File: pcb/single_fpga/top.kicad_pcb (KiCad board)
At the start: 2 copper layers, 320 x 320 mm, 208 parts, among them J1 AXK680337YG, J2 AXK680337YG, J3 AXK680337YG, J4 AXK680337YG, U1 Comment, U10 Comment, U11 Comment, U12 Comment, U13 Comment, U14 Comment, U15 Comment, U16 Comment, U17 Comment, U18 Comment, U19 Comment, U2 Comment, U20 Comment, U21 Comment, U22 Comment, U23 Comment, U24 Comment, U25 Comment, U26 Comment, U27 Comment, U28 Comment, U29 Comment, U3 Comment, U30 Comment, U31 Comment, U32 Comment, U33 Comment, U34 Comment, U35 Comment, U36 Comment, U37 Comment, U38 Comment, U39 Comment, U4 Comment, U40 Comment, U41 Comment, U42 Comment, U43 Comment, U44 Comment, U45 Comment, U46 Comment, U47 Comment, U48 Comment, U49 Comment, U5 Comment, U50 Comment, U51 Comment, U52 Comment, U53 Comment, U54 Comment, U55 Comment, U56 Comment, U57 Comment, U58 Comment, U59 Comment, U6 Comment, U60 Comment, U61 Comment, U62 Comment, U63 Comment, U64 Comment, U65 Comment, U66 Comment, U67 Comment, U68 Comment, U69 Comment, U7 Comment, U70 Comment, U71 Comment, U72 Comment, U73 Comment, U74 Comment, U75 Comment, U76 Comment, U77 Comment, U78 Comment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

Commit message: Fixed mounting holes for Rpi Cam3 Wide.
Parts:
- moved HCAM1 7.97 mm to (258.4, 205.4)
- moved HCAM2 7.97 mm to (279.4, 205.4)
- moved HCAM3 6.20 mm to (258.4, 217.9)
- moved HCAM4 6.20 mm to (279.4, 217.9)
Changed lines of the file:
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@@
 	(footprint "MountingHole_2.2mm_M2"
 		(layer "F.Cu")
-		(at 276.062916 212.612916)
+		(at 279.362916 217.862916)
 		(descr "Mounting Hole 2.2mm, M2, no annular, generated by kicad-footprint-generator mountinghole.py")
 		(tags "mountinghole M2")
@@
 	(footprint "MountingHole_2.2mm_M2"
 		(layer "F.Cu")
-		(at 261.662916 198.112916)
+		(at 258.362915 205.362916)
 		(descr "Mounting Hole 2.2mm, M2, no annular, generated by kicad-footprint-generator mountinghole.py")
 		(tags "mountinghole M2")
@@
 	(footprint "MountingHole_2.2mm_M2"
 		(layer "F.Cu")
-		(at 276.062916 198.112916)
+		(at 279.362916 205.362916)
 		(descr "Mounting Hole 2.2mm, M2, no annular, generated by kicad-footprint-generator mountinghole.py")
 		(tags "mountinghole M2")
@@
 	(footprint "MountingHole_2.2mm_M2"
 		(layer "F.Cu")
-		(at 261.662916 212.612916)
+		(at 258.362915 217.862916)
 		(descr "Mounting Hole 2.2mm, M2, no annular, generated by kicad-footprint-generator mountinghole.py")
 		(tags "mountinghole M2")

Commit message: Fixed.
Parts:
- added U100: PW0016A_N, PW0016A_N, F.Cu at (44.9, 75.0)
- added U101: PW0016A_N, PW0016A_N, F.Cu at (1.34, 87.4)
- added U102: PW0016A_N, PW0016A_N, F.Cu at (-42.5, 76.4)
- added U103: PW0016A_N, PW0016A_N, F.Cu at (-75.0, 44.9)
- added U104: PW0016A_N, PW0016A_N, F.Cu at (-87.4, 1.34)
- added U105: PW0016A_N, PW0016A_N, F.Cu at (-76.4, -42.5)
- added U106: PW0016A_N, PW0016A_N, F.Cu at (-44.9, -75.0)
- added U107: PW0016A_N, PW0016A_N, F.Cu at (-1.34, -87.4)
- added U108: PW0016A_N, PW0016A_N, F.Cu at (42.5, -76.4)
- added U109: PW0016A_N, PW0016A_N, F.Cu at (75.0, -44.9)
- added U110: PW0016A_N, PW0016A_N, F.Cu at (87.4, -1.34)
- added U99: PW0016A_N, PW0016A_N, F.Cu at (76.4, 42.5)

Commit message: Placed 1:8 clock drivers.
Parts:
- U100, U101, U102, U103, U104, U105, U106, U107, U108, U109, U110, U99: footprint PW0016A_N -> CDCLVC1108:PW0016A_N
- moved U101 338.3 mm to (270.2, 292.8)
- moved U109 338.3 mm to (343.9, 160.5)
- moved U100 338.3 mm to (313.7, 280.4)
- moved U103 338.3 mm to (193.8, 250.2)
- moved U104 338.3 mm to (181.4, 206.7)
- moved U106 338.3 mm to (224.0, 130.3)
- moved U107 338.3 mm to (267.5, 117.9)
- moved U108 338.3 mm to (311.4, 129.0)
- moved U99 338.3 mm to (345.2, 247.9)
- moved U102 338.3 mm to (226.3, 281.7)
- moved U105 338.3 mm to (192.5, 162.8)
- moved U110 338.3 mm to (356.3, 204.0)

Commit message: Rotated clock drivers to all up.
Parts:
- turned U104 to 0 degrees
- turned U101 to 0 degrees
- turned U107 to 0 degrees
- turned U110 to 0 degrees
- turned U100 to 0 degrees
- turned U102 to 0 degrees
- turned U103 to 0 degrees
- turned U105 to 0 degrees
- turned U106 to 0 degrees
- turned U108 to 0 degrees
- turned U109 to 0 degrees
- turned U99 to 0 degrees

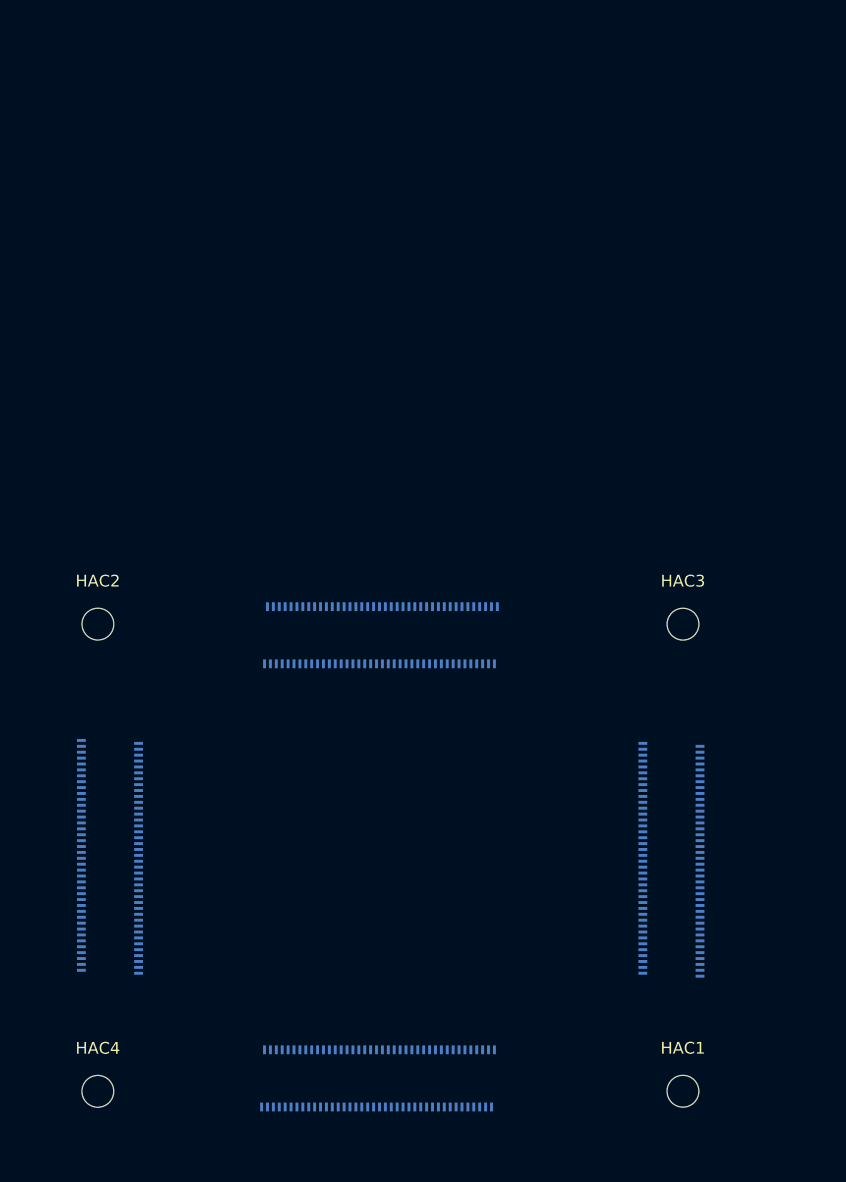
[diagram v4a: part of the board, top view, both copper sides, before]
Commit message: Reorganized sheets for two-boards. Fixed connector off-grid problems.
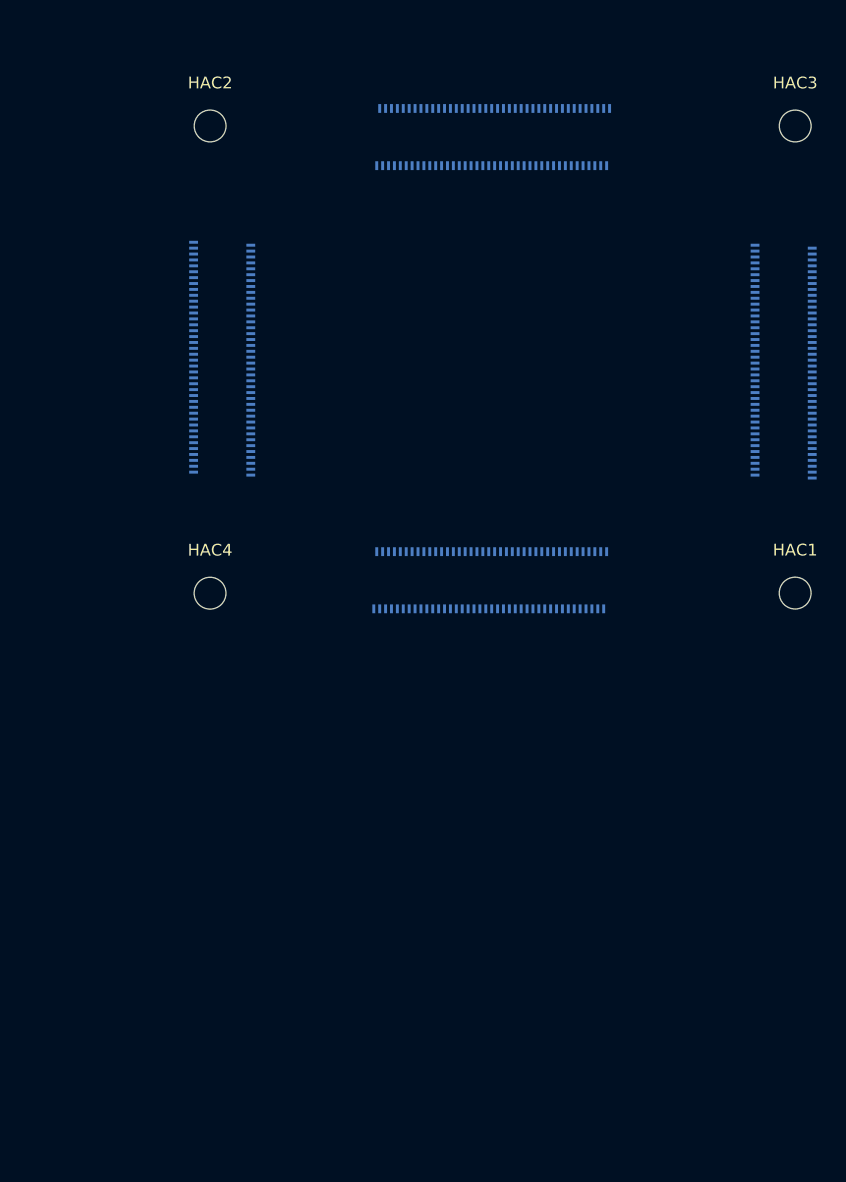
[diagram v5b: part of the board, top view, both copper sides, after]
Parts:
- moved HAC1 43.3 mm to (553.1, 237.7)
- moved HAC2 43.3 mm to (503.5, 198.1)
- moved HAC3 43.3 mm to (553.1, 198.1)
- moved HAC4 43.3 mm to (503.5, 237.7)
- moved J2 43.3 mm to (527.4, 236.6)
- moved J3 43.3 mm to (504.5, 217.9)
- moved J4 43.3 mm to (527.4, 199.0)
- moved J1 43.3 mm to (552.1, 217.9)
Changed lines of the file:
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@@
 	(footprint "MountingHole_2.7mm_M2.5"
 		(layer "F.Cu")
-		(at 543.585321 279.958505)
+		(at 553.104136 237.70183)
 		(descr "Mounting Hole 2.7mm, M2.5, no annular, generated by kicad-footprint-generator mountinghole.py")
 		(tags "mountinghole M2.5")
@@
 	(footprint "MountingHole_2.7mm_M2.5"
 		(layer "F.Cu")
-		(at 493.953721 279.966104)
+		(at 503.472536 237.709429)
 		(descr "Mounting Hole 2.7mm, M2.5, no annular, generated by kicad-footprint-generator mountinghole.py")
 		(tags "mountinghole M2.5")
@@
 	(footprint "MountingHole_2.7mm_M2.5"
 		(layer "F.Cu")
-		(at 493.958821 240.334504)
+		(at 503.477636 198.077829)
 		(descr "Mounting Hole 2.7mm, M2.5, no annular, generated by kicad-footprint-generator mountinghole.py")
 		(tags "mountinghole M2.5")
@@
 	(footprint "MountingHole_2.7mm_M2.5"
 		(layer "F.Cu")
-		(at 543.590421 240.337004)
+		(at 553.109236 198.080329)
 		(descr "Mounting Hole 2.7mm, M2.5, no annular, generated by kicad-footprint-generator mountinghole.py")
 		(tags "mountinghole M2.5")
@@
 	(footprint "AXK680337YG"
 		(layer "B.Cu")
-		(at 517.842422 241.276804)
+		(at 527.361237 199.020129)
 		(descr "Panasonic AXK680337YG P5K-series 80-pin/0.5mm-pitch board-to-board HEADER, 3.0mm mated height. Real dimensions from Panasonic/Mouser's own P5K/P5KS catalog PDF (mouser.com/catalog/specsheets/AXK.pdf), read directly: body 23.20 x 4.60mm (A x width), pin field 19.50mm (B, = (40-1)*0.5mm exactly). Land pattern real: 40 pins/row x 2 rows, 0.5mm pitch, rows staggered by 0.25mm (half pitch, per the catalog's own 'Recommended PC board pattern' drawing), pad 0.25 x 0.75mm, total footprint span 5.60mm (consistent across every land-pattern drawing in the catalog). Pin numbering (1-80 sequential by row) is an ASSUMED convention, not independently verified against a real pin-1 diagram -- the catalog's own orientation key is a chamfered body corner (reproduced here on F.SilkS near pin 1) rather than a numbered pinout drawing. Mates with the ALINX AC7200 module's own AXK580137YG sockets (module-side part number CONFIRMED via ALINX's real schematic, docs/AC7200_Schematic.pdf page 12) -- see ../AC7200/AC7200_README.md.")
 		(tags "Panasonic AXK680337YG P5K board-to-board 80pin 0.5mm")
@@
 	(footprint "AXK680337YG"
 		(layer "B.Cu")
-		(at 494.982421 260.199804 90)
+		(at 504.501236 217.943129 90)
 		(descr "Panasonic AXK680337YG P5K-series 80-pin/0.5mm-pitch board-to-board HEADER, 3.0mm mated height. Real dimensions from Panasonic/Mouser's own P5K/P5KS catalog PDF (mouser.com/catalog/specsheets/AXK.pdf), read directly: body 23.20 x 4.60mm (A x width), pin field 19.50mm (B, = (40-1)*0.5mm exactly). Land pattern real: 40 pins/row x 2 rows, 0.5mm pitch, rows staggered by 0.25mm (half pitch, per the catalog's own 'Recommended PC board pattern' drawing), pad 0.25 x 0.75mm, total footprint span 5.60mm (consistent across every land-pattern drawing in the catalog). Pin numbering (1-80 sequential by row) is an ASSUMED convention, not independently verified against a real pin-1 diagram -- the catalog's own orientation key is a chamfered body corner (reproduced here on F.SilkS near pin 1) rather than a numbered pinout drawing. Mates with the ALINX AC7200 module's own AXK580137YG sockets (module-side part number CONFIRMED via ALINX's real schematic, docs/AC7200_Schematic.pdf page 12) -- see ../AC7200/AC7200_README.md.")
 		(tags "Panasonic AXK680337YG P5K board-to-board 80pin 0.5mm")
@@
 	(footprint "AXK680337YG"
 		(layer "B.Cu")
-		(at 542.607421 260.199804 -90)
+		(at 552.126236 217.943129 -90)
 		(descr "Panasonic AXK680337YG P5K-series 80-pin/0.5mm-pitch board-to-board HEADER, 3.0mm mated height. Real dimensions from Panasonic/Mouser's own P5K/P5KS catalog PDF (mouser.com/catalog/specsheets/AXK.pdf), read directly: body 23.20 x 4.60mm (A x width), pin field 19.50mm (B, = (40-1)*0.5mm exactly). Land pattern real: 40 pins/row x 2 rows, 0.5mm pitch, rows staggered by 0.25mm (half pitch, per the catalog's own 'Recommended PC board pattern' drawing), pad 0.25 x 0.75mm, total footprint span 5.60mm (consistent across every land-pattern drawing in the catalog). Pin numbering (1-80 sequential by row) is an ASSUMED convention, not independently verified against a real pin-1 diagram -- the catalog's own orientation key is a chamfered body corner (reproduced here on F.SilkS near pin 1) rather than a numbered pinout drawing. Mates with the ALINX AC7200 module's own AXK580137YG sockets (module-side part number CONFIRMED via ALINX's real schematic, docs/AC7200_Schematic.pdf page 12) -- see ../AC7200/AC7200_README.md.")
 		(tags "Panasonic AXK680337YG P5K board-to-board 80pin 0.5mm")
@@
 	(footprint "AXK680337YG"
 		(layer "B.Cu")
-		(at 517.842422 278.868804 180)
+		(at 527.361237 236.612129 180)
 		(descr "Panasonic AXK680337YG P5K-series 80-pin/0.5mm-pitch board-to-board HEADER, 3.0mm mated height. Real dimensions from Panasonic/Mouser's own P5K/P5KS catalog PDF (mouser.com/catalog/specsheets/AXK.pdf), read directly: body 23.20 x 4.60mm (A x width), pin field 19.50mm (B, = (40-1)*0.5mm exactly). Land pattern real: 40 pins/row x 2 rows, 0.5mm pitch, rows staggered by 0.25mm (half pitch, per the catalog's own 'Recommended PC board pattern' drawing), pad 0.25 x 0.75mm, total footprint span 5.60mm (consistent across every land-pattern drawing in the catalog). Pin numbering (1-80 sequential by row) is an ASSUMED convention, not independently verified against a real pin-1 diagram -- the catalog's own orientation key is a chamfered body corner (reproduced here on F.SilkS near pin 1) rather than a numbered pinout drawing. Mates with the ALINX AC7200 module's own AXK580137YG sockets (module-side part number CONFIRMED via ALINX's real schematic, docs/AC7200_Schematic.pdf page 12) -- see ../AC7200/AC7200_README.md.")
 		(tags "Panasonic AXK680337YG P5K board-to-board 80pin 0.5mm")
